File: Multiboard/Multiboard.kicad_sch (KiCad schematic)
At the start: 6 parts, among them J1 Conn_01x20_Socket, J2 Conn_01x20_Socket, SW1 BOOT0, U1 STM32F411RET6, U2 LCMXO2-1200HC-4TG100C

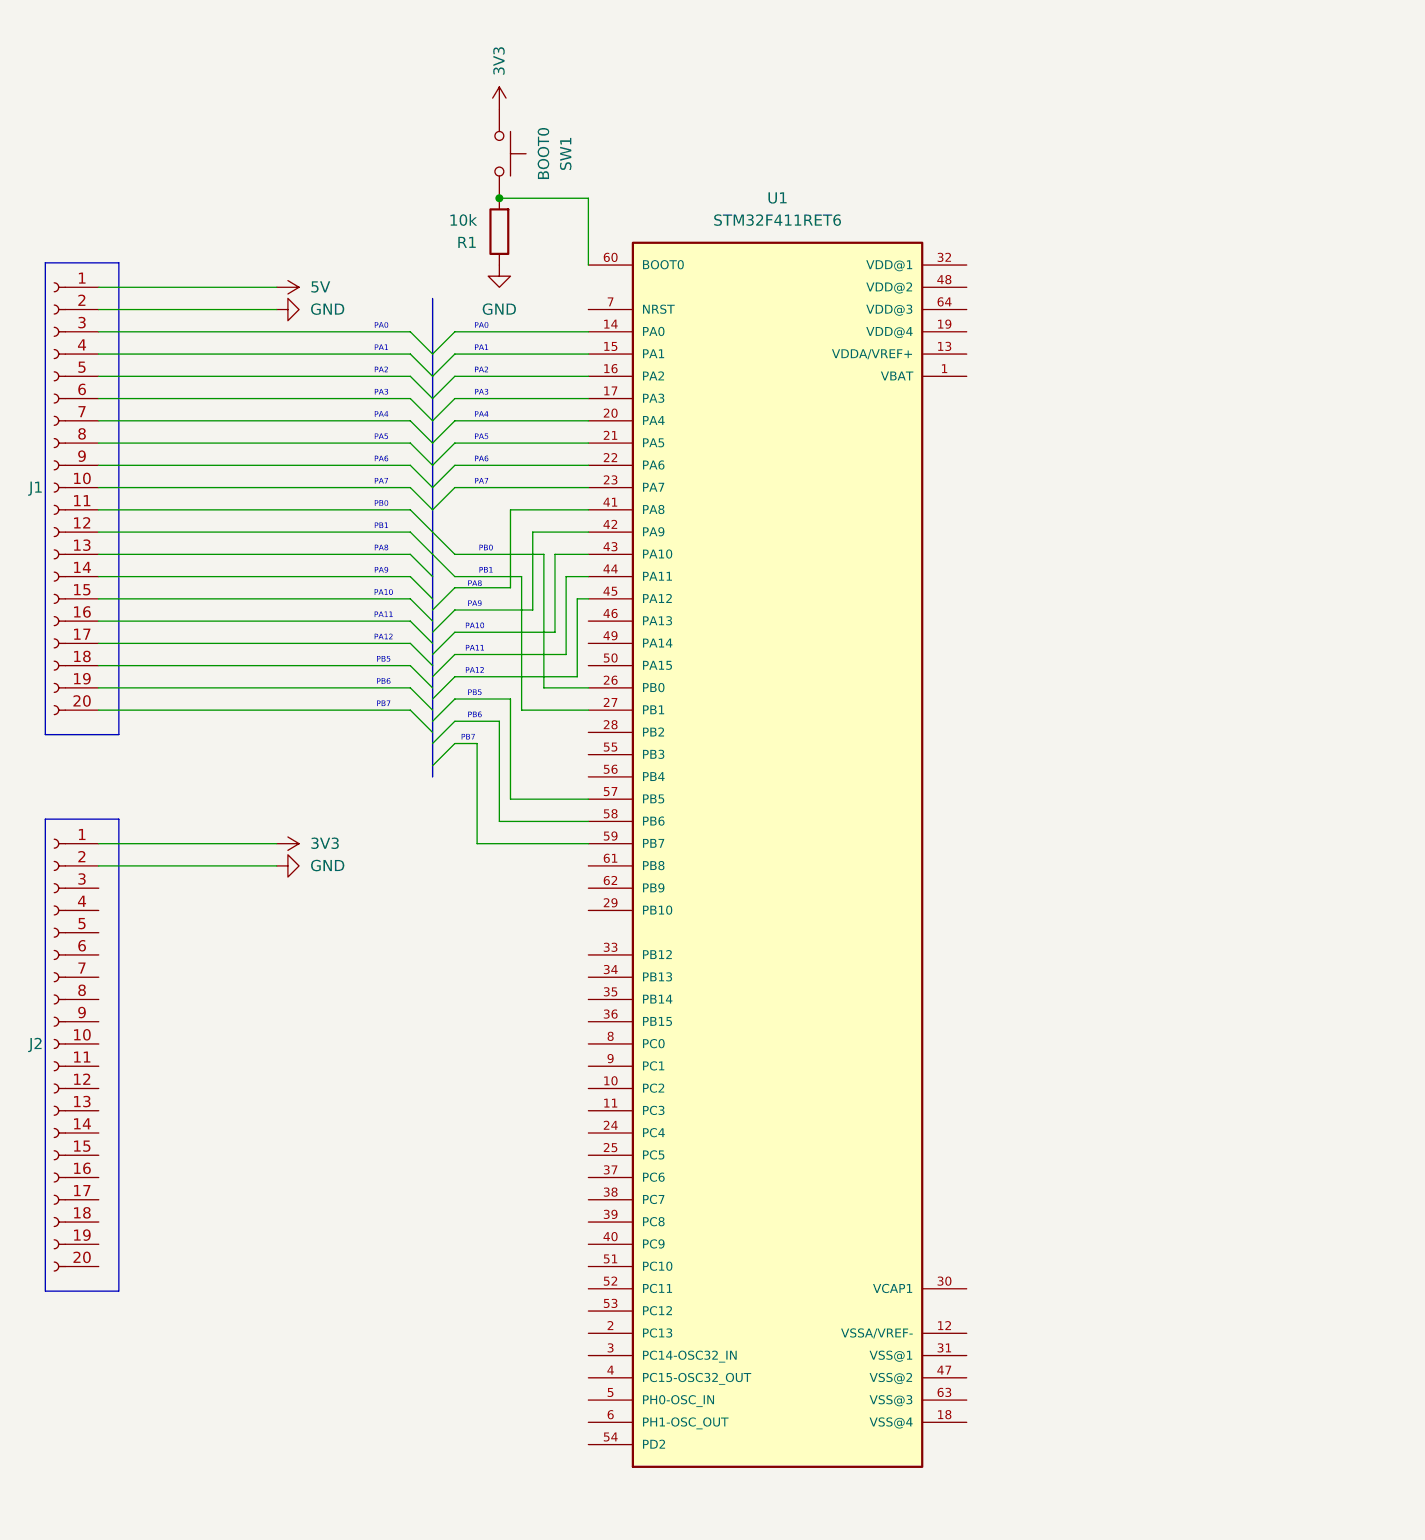
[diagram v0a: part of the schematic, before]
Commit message: Wired second header row and added 1 ch bid level shifter symbol
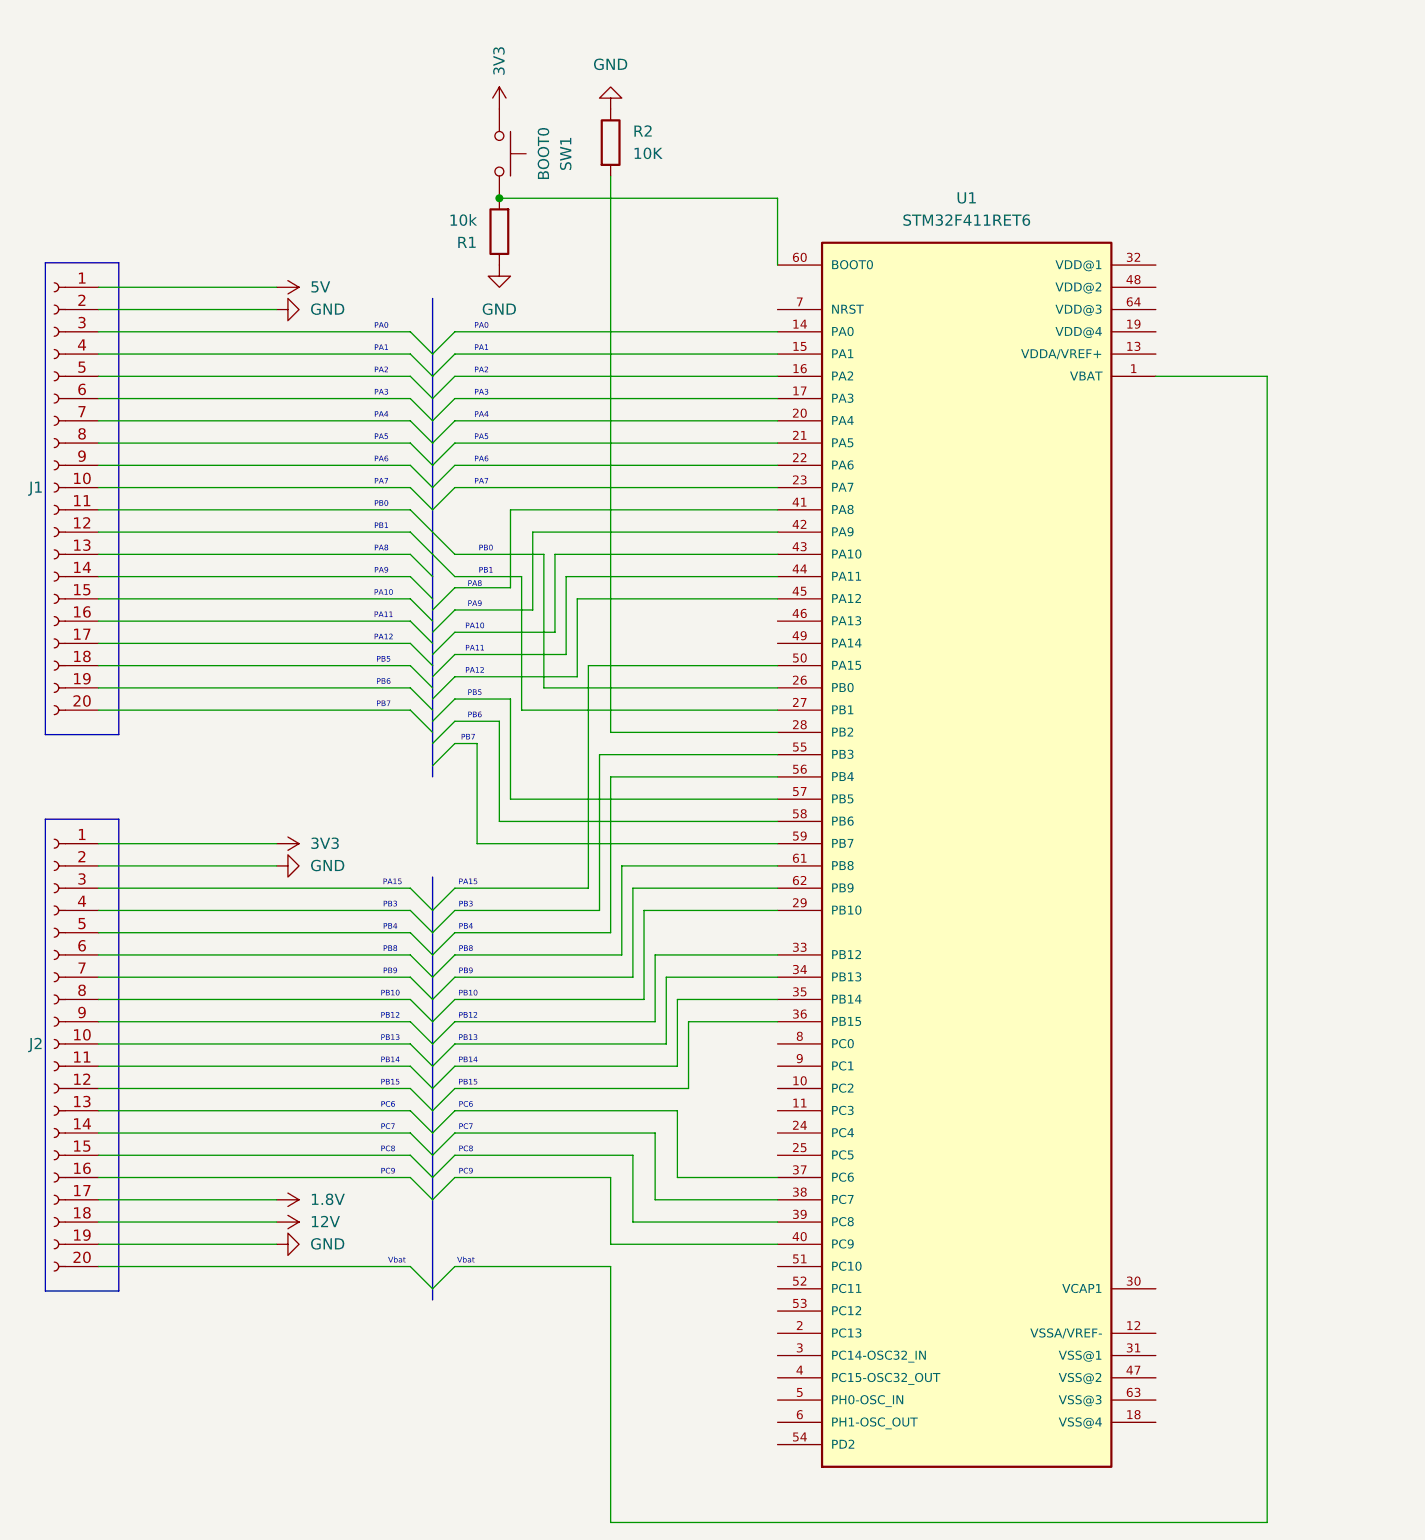
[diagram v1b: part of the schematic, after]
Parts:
- added R2: 10K, symbol Device:R
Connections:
- net GND: now also J2.19 (Pin_19), R2.1
- net 1.8V: now reaches J2.17 (Pin_17)
- net 12V: now reaches J2.18 (Pin_18)
- net at U1.28 (PB2): now also R2.2
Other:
- note added: "PA15"
- note added: "PB10"
- note added: "PB12"
- note added: "PB13"
- note added: "PB14"
- note added: "PB15"
- note added: "PB3"
- note added: "PB4"
- note added: "PB8"
- note added: "PB9"
- note added: "PC6"
- note added: "PC7"
- note added: "PC8"
- note added: "PC9"
- note added: "Vbat"
- moved on the sheet: U1

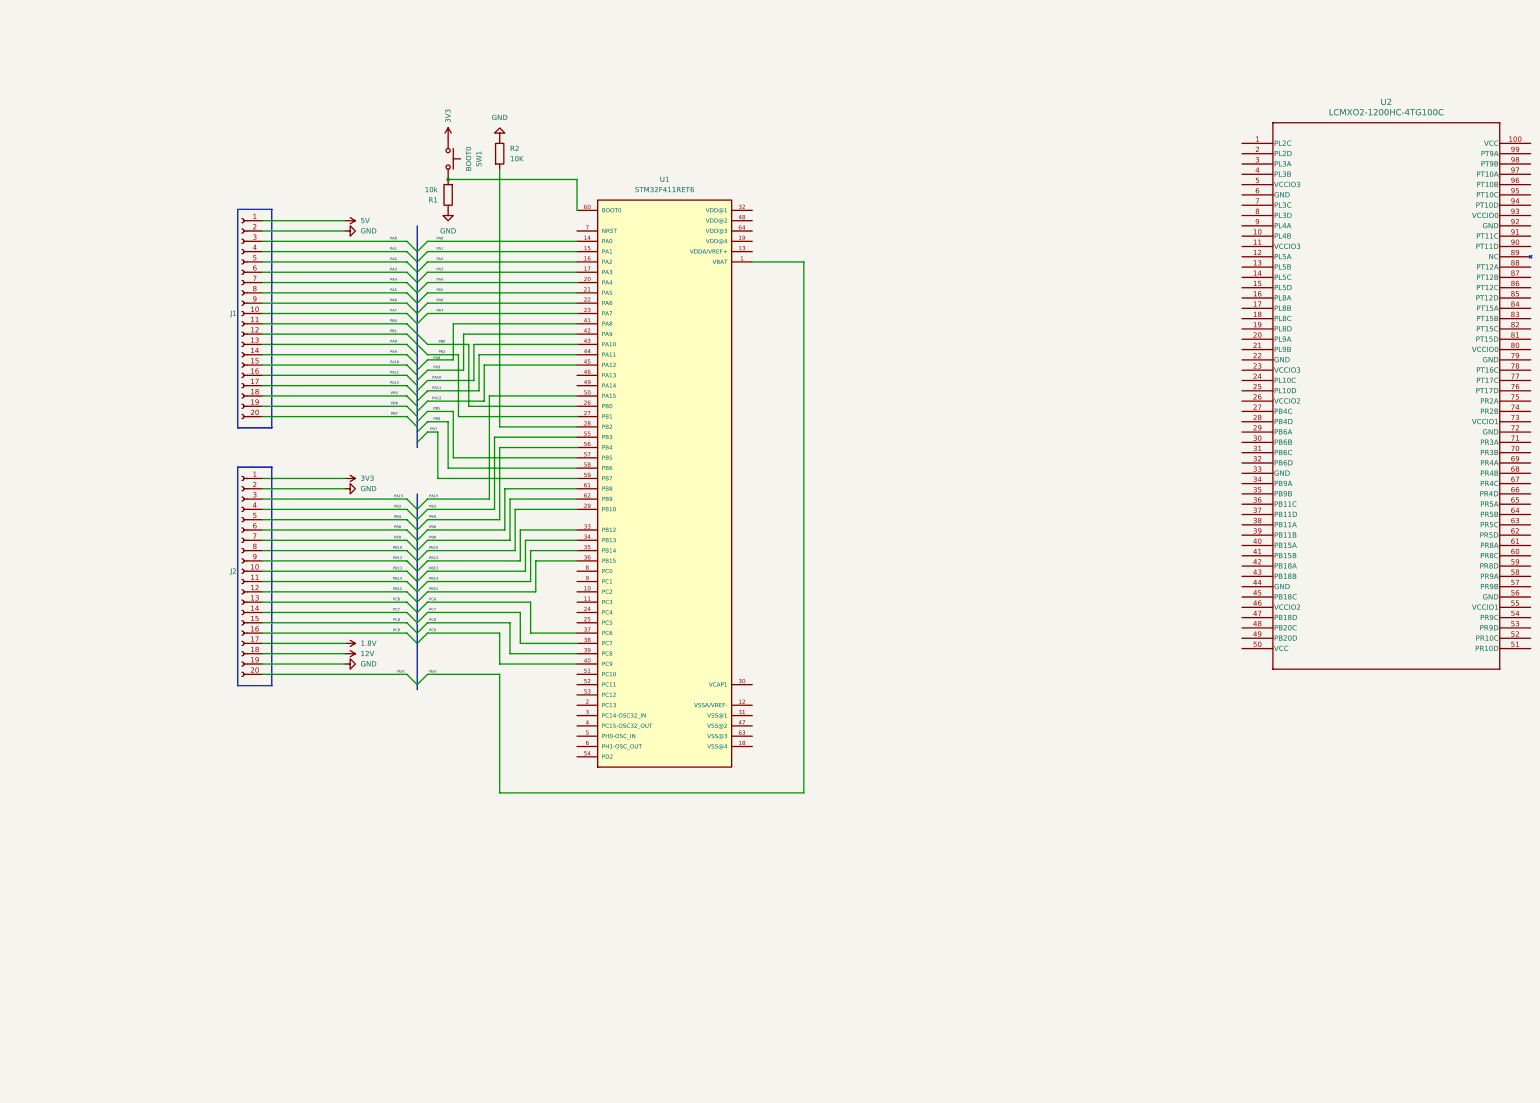
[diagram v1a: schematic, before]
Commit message: Added reset, power, rtc, level shifter and oscilator circuits
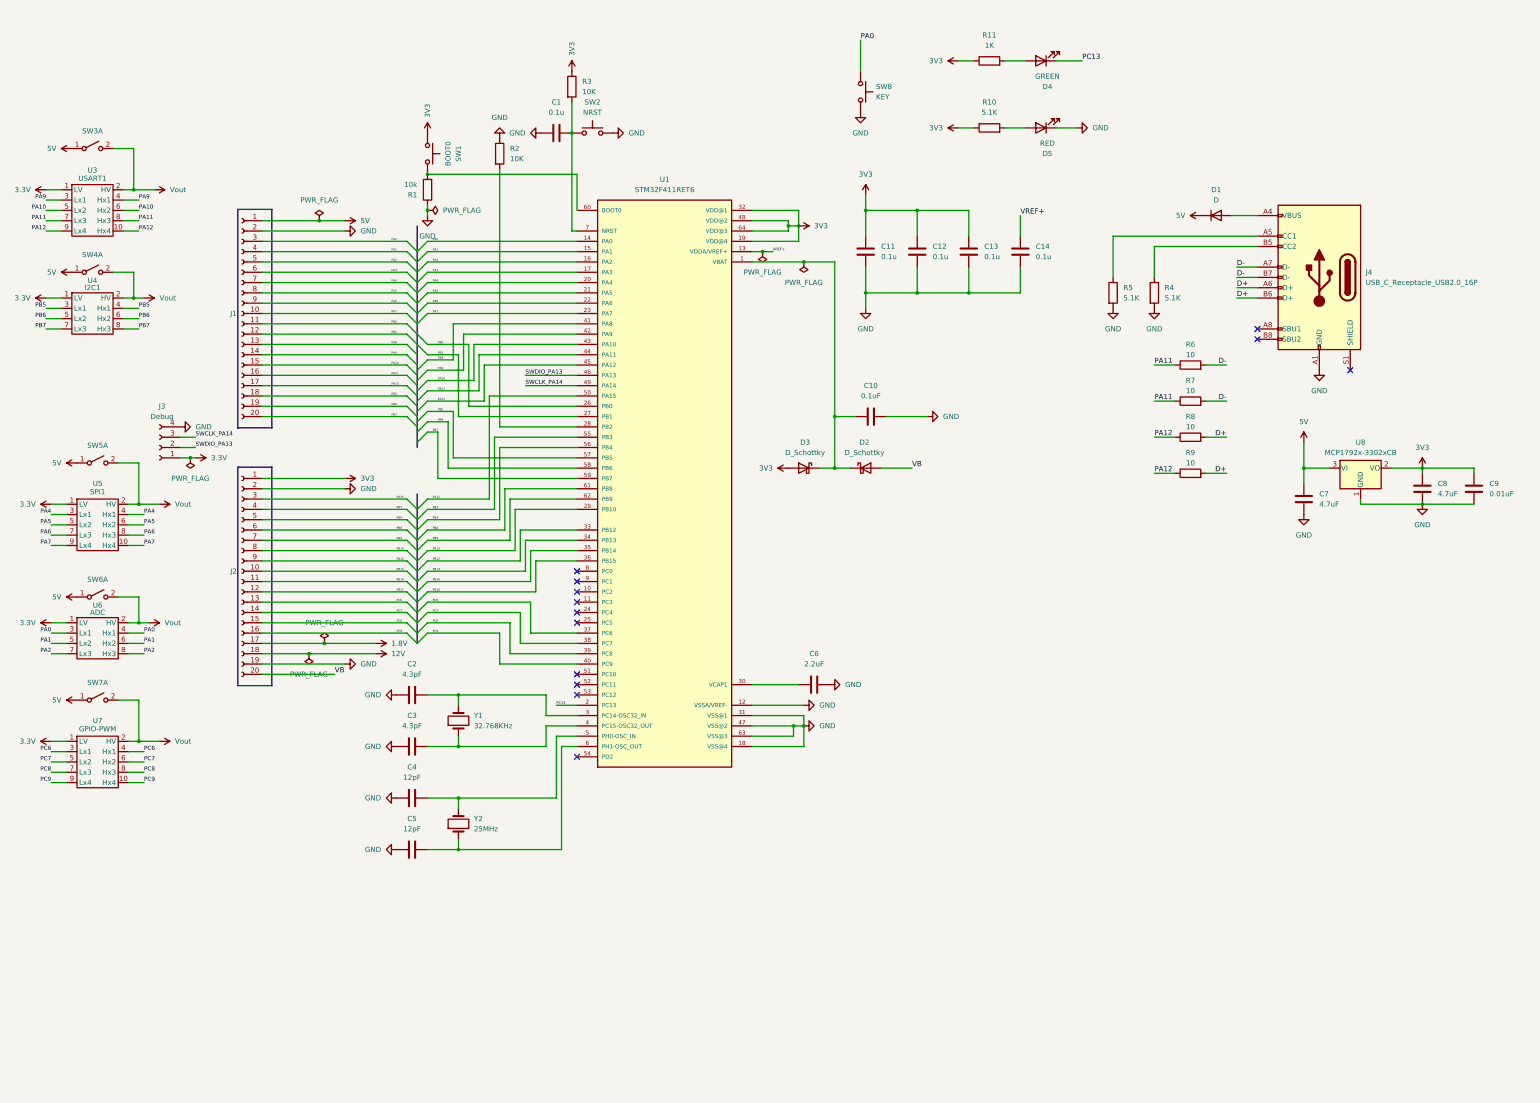
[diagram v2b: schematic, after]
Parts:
- removed U2: LCMXO2-1200HC-4TG100C, TQFP100_LAT, symbol LCMXO2-1200HC-4TG100C:LCMXO2-1200HC-4TG100C
- added C1, C11, C12, C13, C14: 0.1u, symbol Device:C
- added C10: 0.1uF, symbol Device:C
- added C2, C3: 4.3pF, symbol Device:C
- added C4, C5: 12pF, symbol Device:C
- added C6: 2.2uF, symbol Device:C
- added C7, C8: 4.7uF, symbol Device:C
- added C9: 0.01uF, symbol Device:C
- added D1: D, symbol Device:D
- added D2, D3: D_Schottky, symbol Device:D_Schottky
- added D4: GREEN, symbol Device:LED
- added D5: RED, symbol Device:LED
- added J3: Debug, symbol Connector:Conn_01x04_Socket
- added J4: USB_C_Receptacle_USB2.0_16P, symbol Connector:USB_C_Receptacle_USB2.0_16P
- added R10, R4, R5: 5.1K, symbol Device:R
- added R11: 1K, symbol Device:R
- added R3: 10K, symbol Device:R
- added R6, R7, R8, R9: 10, symbol Device:R
- added SW2: NRST, symbol Switch:SW_Push
- added SW3, SW4, SW5, SW6, SW7: ~, symbol Switch:SW_DPST_x2
- added SW8: KEY, symbol Switch:SW_Push
- added U3: USART1, symbol Level_Shifter:Level_Shifter_4_BD
- added U4: I2C1, symbol Level_Shifter:Level_Shifter_3_BD
- added U5: SPI1, symbol Level_Shifter:Level_Shifter_4_BD
- added U6: ADC, symbol Level_Shifter:Level_Shifter_3_BD
- added U7: GPIO-PWM, symbol Level_Shifter:Level_Shifter_4_BD
- added U8: MCP1792x-3302xCB, Package_DFN_QFN:DFN-6-1EP_3x3mm_P0.95mm_EP1.7x2.6mm, symbol Regulator_Linear:MCP1792x-3302xCB
- added Y1: 32.768KHz, symbol Device:Crystal
- added Y2: 25MHz, symbol Device:Crystal
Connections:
- net 3V3: now also U1.19 (VDD@4), U1.32 (VDD@1), U1.48 (VDD@2), U1.64 (VDD@3), C11.1, C12.1, C13.1, C8.1, C9.1, D3.2 (A), R10.1, R11.1, R3.1, U8.2 (VO)
- net 5V: now also C7.1, D1.1 (K), SW3.1 (A), SW4.1 (A), SW5.1 (A), SW6.1 (A), SW7.1 (A), U8.3 (VI)
- net GND: now also U1.12 (VSSA/VREF-), U1.18 (VSS@4), U1.31 (VSS@1), U1.47 (VSS@2), U1.63 (VSS@3), C1.2, C10.2, C11.2, C12.2, C13.2, C14.2, C2.1, C3.1, C4.1, C5.1, C6.2, C7.2, C8.2, C9.2, D5.1 (K), J3.4 (Pin_4), J4.A1 (GND), J4.A12 (GND), J4.B1 (GND), J4.B12 (GND), R4.2, R5.2, SW2.2, SW8.2, U8.1 (GND)
- net PB13: now reaches J2.10 (Pin_10)
- net PB13: now also U1.34 (PB13)
- net PB14: now reaches J2.11 (Pin_11)
- net PB14: now also U1.35 (PB14)
- net PB15: now reaches J2.12 (Pin_12)
- net PB15: now also U1.36 (PB15)
- net PC6: now reaches J2.13 (Pin_13)
- net PC6: now also U1.37 (PC6), U7.3 (Lx1), U7.4 (Hx1)
- net PC7: now reaches J2.14 (Pin_14)
- net PC7: now also U1.38 (PC7), U7.5 (Lx2), U7.6 (Hx2)
- net PC8: now reaches J2.15 (Pin_15)
- net PC8: now also U1.39 (PC8), U7.7 (Lx3), U7.8 (Hx3)
- net PC9: now reaches J2.16 (Pin_16)
- net PC9: now also U1.40 (PC9), U7.10 (Hx4), U7.9 (Lx4)
- net VB: now reaches J2.20 (Pin_20)
- net VB: now also D2.2 (A)
- net PA15: now reaches J2.3 (Pin_3)
- net PA15: now also U1.50 (PA15)
- net PB3: now reaches J2.4 (Pin_4)
- net PB3: now also U1.55 (PB3)
- net PB4: now reaches J2.5 (Pin_5)
- net PB4: now also U1.56 (PB4)
- net PB8: now reaches J2.6 (Pin_6)
- net PB8: now also U1.61 (PB8)
- net PB9: now reaches J2.7 (Pin_7)
- net PB9: now also U1.62 (PB9)
- net PB10: now reaches J2.8 (Pin_8)
- net PB10: now also U1.29 (PB10)
- net PB12: now reaches J2.9 (Pin_9)
- net PB12: now also U1.33 (PB12)
- net at U1.1 (VBAT): now also C10.1, D2.1 (K), D3.1 (K)
- net VREF+: now reaches U1.13 (VDDA/VREF+)
- net VREF+: now also C14.1
- net PA0: now reaches U1.14 (PA0)
- net PA0: now also J1.3 (Pin_3), SW8.1, U6.3 (Lx1), U6.4 (Hx1)
- net PA1: now reaches U1.15 (PA1)
- net PA1: now also J1.4 (Pin_4), U6.5 (Lx2), U6.6 (Hx2)
- net PA2: now reaches U1.16 (PA2)
- net PA2: now also J1.5 (Pin_5), U6.7 (Lx3), U6.8 (Hx3)
- net PA3: now reaches U1.17 (PA3)
- net PA3: now also J1.6 (Pin_6)
- net PC13: now reaches U1.2 (PC13)
- net PC13: now also D4.1 (K)
- net PA4: now reaches U1.20 (PA4)
- net PA4: now also J1.7 (Pin_7), U5.3 (Lx1), U5.4 (Hx1)
- net PA5: now reaches U1.21 (PA5)
- net PA5: now also J1.8 (Pin_8), U5.5 (Lx2), U5.6 (Hx2)
- net PA6: now reaches U1.22 (PA6)
- net PA6: now also J1.9 (Pin_9), U5.7 (Lx3), U5.8 (Hx3)
- net PA7: now reaches U1.23 (PA7)
- net PA7: now also J1.10 (Pin_10), U5.10 (Hx4), U5.9 (Lx4)
- net PB0: now reaches U1.26 (PB0)
- net PB0: now also J1.11 (Pin_11)
- net PB1: now reaches U1.27 (PB1)
- net PB1: now also J1.12 (Pin_12)
- net at U1.3 (PC14-OSC32_IN): now also C2.2, Y1.2
- net at U1.30 (VCAP1): now also C6.1
- net at U1.4 (PC15-OSC32_OUT): now also C3.2, Y1.1
- net PA8: now reaches U1.41 (PA8)
- net PA8: now also J1.13 (Pin_13)
- net PA9: now reaches U1.42 (PA9)
- net PA9: now also J1.14 (Pin_14), U3.3 (Lx1), U3.4 (Hx1)
- net PA10: now reaches U1.43 (PA10)
- net PA10: now also J1.15 (Pin_15), U3.5 (Lx2), U3.6 (Hx2)
- net PA11: now reaches U1.44 (PA11)
- net PA11: now also J1.16 (Pin_16), R6.1, R7.1, U3.7 (Lx3), U3.8 (Hx3)
- net PA12: now reaches U1.45 (PA12)
- net PA12: now also J1.17 (Pin_17), R8.1, R9.1, U3.10 (Hx4), U3.9 (Lx4)
- net SWDIO_PA13: now reaches U1.46 (PA13)
- net SWDIO_PA13: now also J3.2 (Pin_2)
- net SWCLK_PA14: now reaches U1.49 (PA14)
- net SWCLK_PA14: now also J3.3 (Pin_3)
- net at U1.5 (PH0-OSC_IN): now also C4.2, Y2.2
- net PB5: now reaches U1.57 (PB5)
- net PB5: now also J1.18 (Pin_18), U4.3 (Lx1), U4.4 (Hx1)
- net PB6: now reaches U1.58 (PB6)
- net PB6: now also J1.19 (Pin_19), U4.5 (Lx2), U4.6 (Hx2)
- net PB7: now reaches U1.59 (PB7)
- net PB7: now also J1.20 (Pin_20), U4.7 (Lx3), U4.8 (Hx3)
- net at U1.6 (PH1-OSC_OUT): now also C5.2, Y2.1
- net at U1.7 (NRST): now also C1.1, R3.2, SW2.1
- new net: D5.2 (A), R10.2
- new net: J4.B5 (CC2), R4.1
- new net: D1.2 (A), J4.A4 (VBUS), J4.A9 (VBUS), J4.B4 (VBUS), J4.B9 (VBUS)
- new net: J4.A5 (CC1), R5.1
- new net: D4.2 (A), R11.2
- new net 3.3V: J3.1 (Pin_1), U3.1 (LV), U4.1 (LV), U5.1 (LV), U6.1 (LV), U7.1 (LV)
- new net D+: J4.A6 (D+), J4.B6 (D+), R8.2, R9.2
- new net D-: J4.A7 (D-), J4.B7 (D-), R6.2, R7.2
- new net Vout: SW3.2 (B), SW4.2 (B), SW5.2 (B), SW6.2 (B), SW7.2 (B), U3.2 (HV), U4.2 (HV), U5.2 (HV), U6.2 (HV), U7.2 (HV)
- no-connect marks 0 -> 13
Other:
- note removed: "PA0"
- note removed: "PA1"
- note removed: "PA10"
- note removed: "PA11"
- note removed: "PA12"
- note removed: "PA15"
- note removed: "PA2"
- note removed: "PA3"
- note removed: "PA4"
- note removed: "PA5"
- note removed: "PA6"
- note removed: "PA7"
- note removed: "PA8"
- note removed: "PA9"
- note removed: "PB0"
- note removed: "PB1"
- note removed: "PB10"
- note removed: "PB12"
- note removed: "PB13"
- note removed: "PB14"
- note removed: "PB15"
- note removed: "PB3"
- note removed: "PB4"
- note removed: "PB5"
- note removed: "PB6"
- note removed: "PB7"
- note removed: "PB8"
- note removed: "PB9"
- note removed: "PC6"
- note removed: "PC7"
- note removed: "PC8"
- note removed: "PC9"
- note removed: "Vbat"
- moved on the sheet: R1, SW1
